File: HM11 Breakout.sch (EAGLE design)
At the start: 7 parts

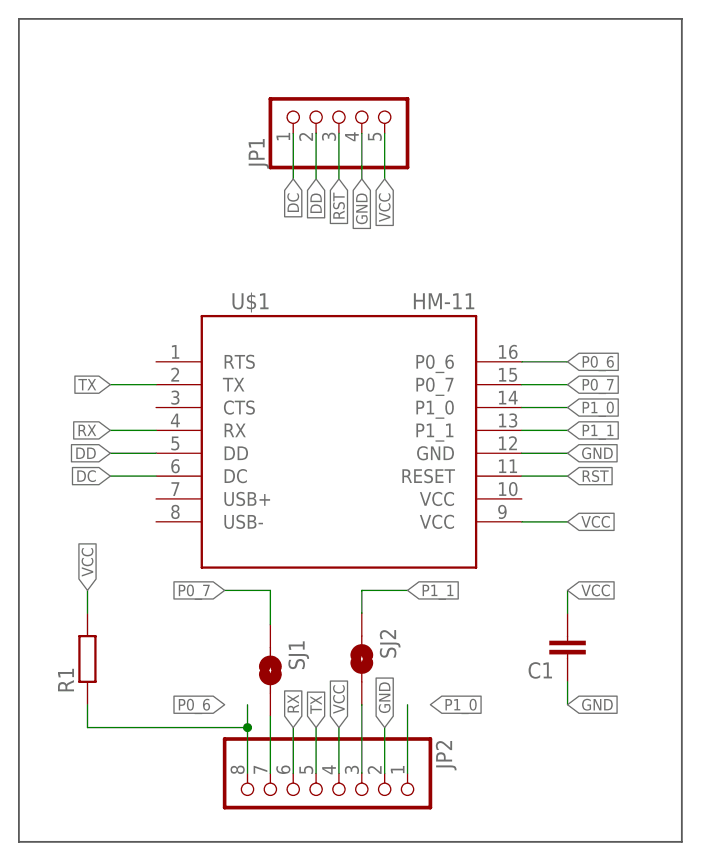
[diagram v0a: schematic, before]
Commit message: add version & attribution text
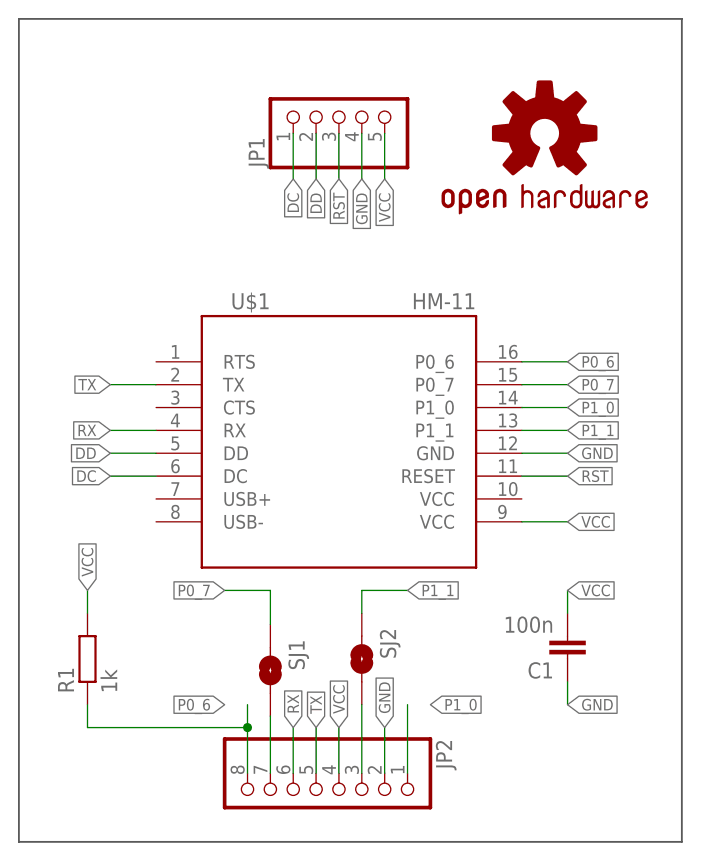
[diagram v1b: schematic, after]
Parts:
- added LOGO1: OSHW-LOGOM, Master 2016:OSHW-LOGOM
- C1: value (none) -> 100n
- R1: value (none) -> 1k
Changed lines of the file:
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@@
 <part name="SJ1" library="Master 2016" deviceset="SOLDERJUMPER" device="TRACE"/>
 <part name="SJ2" library="Master 2016" deviceset="SOLDERJUMPER" device="TRACE"/>
-<part name="R1" library="rcl" library_urn="urn:adsk.eagle:library:334" deviceset="R-EU_" device="R1206" package3d_urn="urn:adsk.eagle:package:23540/2"/>
-<part name="C1" library="Master 2016" deviceset="C-EU" device="1206"/>
+<part name="R1" library="rcl" library_urn="urn:adsk.eagle:library:334" deviceset="R-EU_" device="R1206" package3d_urn="urn:adsk.eagle:package:23540/2" value="1k"/>
+<part name="C1" library="Master 2016" deviceset="C-EU" device="1206" value="100n"/>
+<part name="LOGO1" library="Master 2016" deviceset="OSHW-LOGO" device="M"/>
 </parts>
 <sheets>
@@
 <attribute name="VALUE" x="64.516" y="45.339" size="1.778" layer="96" rot="R180"/>
 </instance>
+<instance part="LOGO1" gate="G$1" x="63.5" y="99.06" smashed="yes"/>
 </instances>
 <busses>
@@
 </sheet>
 </sheets>
+<errors>
+</errors>
 </schematic>
 </drawing>
